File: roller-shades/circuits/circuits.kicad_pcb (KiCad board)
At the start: 2 copper layers, 40 x 55 mm, 38 parts, among them J1 USB_C_Receptacle_USB2.0, J2 SSD1306 connector, M1 Motor_DC, Q1 BC807, Q2 BC817, Q3 BC807, Q4 BC817, SW1 Rotary_Encoder_Switch, U1 AMS1117-3.3, U2 MCP9804_MSOP, U3 ESP-12F

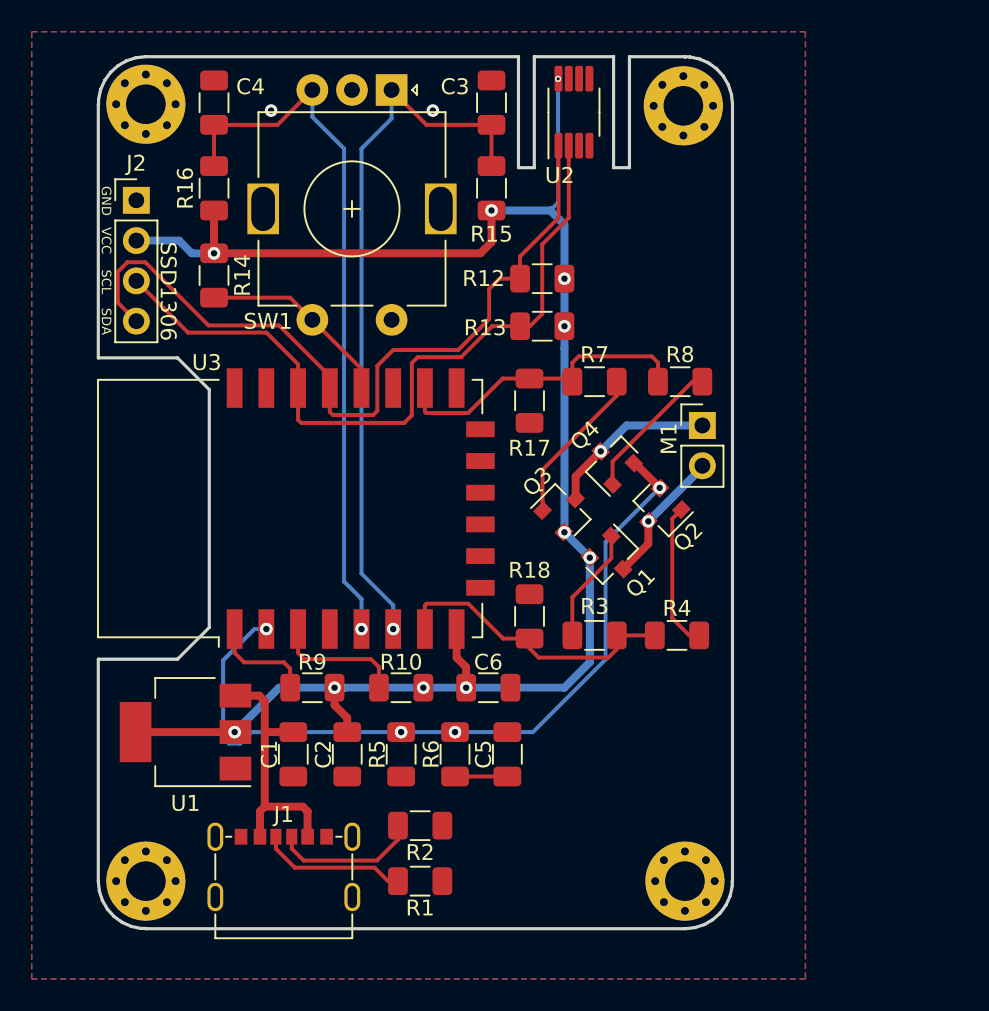
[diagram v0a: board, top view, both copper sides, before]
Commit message: working on driver board using kicad stepup for freecad
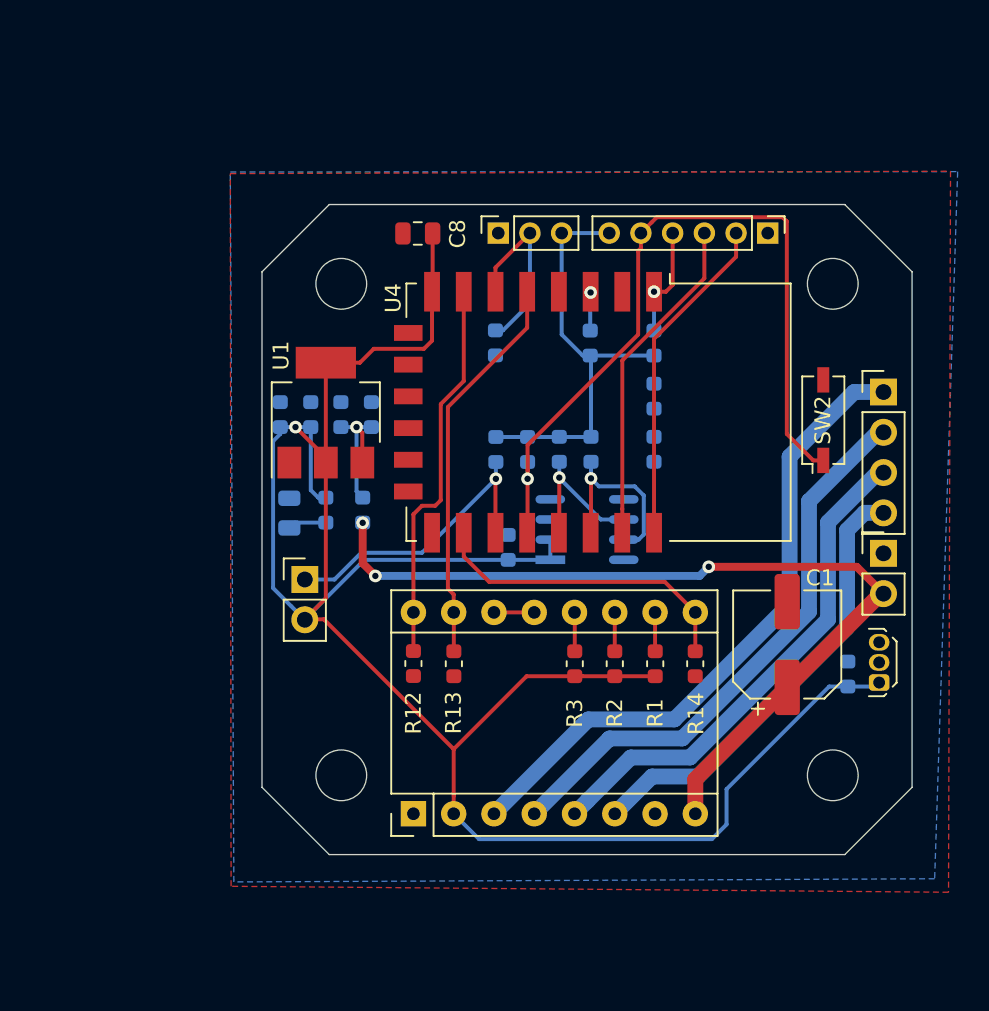
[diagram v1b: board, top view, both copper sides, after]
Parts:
- removed M1: Motor_DC, Connector_PinHeader_2.54mm:PinHeader_1x02_P2.54mm_Vertical
- removed Q1, Q3: BC807, Package_TO_SOT_SMD:SOT-23
- removed Q2, Q4: BC817, Package_TO_SOT_SMD:SOT-23
- removed R17, R18: 10K, Capacitor_SMD:C_1206_3216Metric
- removed REF** (x4): MountingHole_2.5mm_Pad_Via, MountingHole:MountingHole_2.5mm_Pad_Via
- removed SW1: Rotary_Encoder_Switch, Rotary_Encoder:RotaryEncoder_Alps_EC11E-Switch_Vertical_H20mm
- added A1: Pololu_Breakout_A4988, Module:Pololu_Breakout-16_15.2x20.3mm, F.Cu at (49.9, 70.2)
- added C7: 100nF, Capacitor_SMD:C_0603_1608Metric, B.Cu at (43.4, 45.1)
- added C8: 100nF, Fuse:Fuse_0805_2012Metric, F.Cu at (50.1, 33.6)
- added D1: DIODE, Diode_SMD:D_0805_2012Metric, B.Cu at (42.0, 51.3)
- added F1: Fuse, Fuse:Fuse_0603_1608Metric, B.Cu at (46.7, 51.1)
- added J3: PWR, Connector_PinHeader_2.54mm:PinHeader_1x02_P2.54mm_Vertical, F.Cu at (79.5, 53.8)
- added J4: PROG, Connector_PinHeader_2.00mm:PinHeader_1x06_P2.00mm_Vertical, F.Cu at (72.2, 33.6)
- added J5: WINDOW, Connector_PinHeader_2.54mm:PinHeader_1x02_P2.54mm_Vertical, F.Cu at (43.0, 55.5)
- added R11: 10k, Resistor_SMD:R_0603_1608Metric, B.Cu at (57.1, 47.3)
- added SW2: BTN_SW, Button_Switch_SMD:SW_DIP_SPSTx01_Slide_Copal_CHS-01A_W5.08mm_P1.27mm_JPin, F.Cu at (75.7, 45.4)
- added U4: ESP-12F, RF_Module:ESP-12E, F.Cu at (61.5, 44.9)
- C1: value 10µF -> 100µF; footprint Capacitor_SMD:C_1206_3216Metric -> Capacitor_SMD:CP_Elec_6.3x7.7
- C2: value 22µF -> 100nF; footprint Capacitor_SMD:C_1206_3216Metric -> Capacitor_SMD:C_0603_1608Metric; moved to B.Cu
- C3: value 10nF -> 10µF; footprint Capacitor_SMD:C_1206_3216Metric -> Capacitor_SMD:C_0603_1608Metric; moved to B.Cu
- C4: value 10nF -> 100nF; footprint Capacitor_SMD:C_1206_3216Metric -> Capacitor_SMD:C_0603_1608Metric; moved to B.Cu
- C5: value 100p -> 100nF; footprint Capacitor_SMD:C_1206_3216Metric -> Capacitor_SMD:C_0603_1608Metric; moved to B.Cu
- C6: value 100nF -> 10µF; footprint Capacitor_SMD:C_1206_3216Metric -> Capacitor_SMD:C_0603_1608Metric; moved to B.Cu
- J1: value USB_C_Receptacle_USB2.0 -> NEMA17; footprint Connector_USB:USB_C_Receptacle_SHOU_HAN_6P -> Connector_PinHeader_2.54mm:PinHeader_1x04_P2.54mm_Vertical
- J2: value SSD1306 connector -> DS18B20; footprint Connector_PinHeader_2.54mm:PinHeader_1x04_P2.54mm_Vertical -> Connector_PinSocket_2.00mm:PinSocket_1x03_P2.00mm_Vertical
- R1, R2: value 5K1 -> 10k; footprint Capacitor_SMD:C_1206_3216Metric -> Resistor_SMD:R_0603_1608Metric
- R10, R15, R16, R9: value 10K -> 10k; footprint Capacitor_SMD:C_1206_3216Metric -> Resistor_SMD:R_0603_1608Metric; moved to B.Cu
- R12, R13, R14: value 10K -> 10k; footprint Capacitor_SMD:C_1206_3216Metric -> Resistor_SMD:R_0603_1608Metric
- R3: value 1K -> 10k; footprint Capacitor_SMD:C_1206_3216Metric -> Resistor_SMD:R_0603_1608Metric
- R4, R8: value 1K -> 10k; footprint Capacitor_SMD:C_1206_3216Metric -> Resistor_SMD:R_0603_1608Metric; moved to B.Cu
- R5: value 20mR -> 220k; footprint Capacitor_SMD:C_1206_3216Metric -> Resistor_SMD:R_0603_1608Metric; moved to B.Cu
- R6: value 1K -> 100k; footprint Capacitor_SMD:C_1206_3216Metric -> Resistor_SMD:R_0603_1608Metric; moved to B.Cu
- R7: footprint Capacitor_SMD:C_1206_3216Metric -> Resistor_SMD:R_0603_1608Metric; moved to B.Cu
- U2: value MCP9804_MSOP -> AS5601-ASOM; footprint Package_SO:MSOP-8_3x3mm_P0.65mm -> AS5601:Taos-AS5601-ASOM-0-0-0; moved to B.Cu
- U3: value ESP-12F -> DRV5033A1; footprint RF_Module:ESP-12E -> Package_TO_SOT_THT:TO-92Flat
- moved J1 48.2 mm to (79.5, 43.6)
- moved R14 39.0 mm to (67.7, 60.8), turned to 90 degrees
- moved U3 38.7 mm to (79.2, 62.0)
- moved C1 31.9 mm to (73.5, 59.6), turned to 90 degrees
- moved R9 27.9 mm to (61.0, 40.6), turned to 90 degrees
- moved U2 26.3 mm to (60.8, 52.3), turned to 0 degrees
- moved R6 25.8 mm to (65.0, 43.9), turned to 90 degrees
- moved R12 25.6 mm to (49.9, 60.8), turned to 90 degrees
- moved R5 25.0 mm to (65.0, 47.3)
- moved J2 22.9 mm to (55.2, 33.6), turned to 90 degrees
- moved C5 22.1 mm to (77.3, 61.4)
- moved U1 22.0 mm to (44.4, 45.0), turned to 90 degrees
- moved R13 22.0 mm to (52.4, 60.8), turned to 90 degrees
- moved C6 21.7 mm to (41.5, 45.1), turned to 90 degrees
- moved C4 21.2 mm to (45.3, 45.1)
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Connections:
- C1 pad 1: +5V -> VDD
- C3 pad 1: /ESP_IO12 -> Net-(C3-Pad1)
- C4 pad 1: /ESP_IO14 -> Net-(C3-Pad1)
- C5 pad 1: Net-(C5-Pad1) -> +3V3
- J2 pad 2: +3V3 -> /GPIO12
- J2 pad 3: /ESP_IO5 -> +3V3
- R1 pad 1: Net-(J1-PadA5) -> +3V3
- R1 pad 2: GND -> /STPR_MS1
- R10 pad 2: /ESP_EN -> /I2C_SCL
- R12 pad 1: +3V3 -> GND
- R12 pad 2: /ESP_IO4 -> /STPR_DIR
- R13 pad 1: +3V3 -> GND
- R13 pad 2: /ESP_IO5 -> /STPR_STP
- R14 pad 1: +3V3 -> GND
- R14 pad 2: /ESP_IO0 -> /STPR_ENA
- R15 pad 2: /ESP_IO12 -> /GPIO2
- R16 pad 1: +3V3 -> GND
- R16 pad 2: /ESP_IO14 -> /GPIO12
- R2 pad 1: Net-(J1-PadB5) -> +3V3
- R2 pad 2: GND -> /STPR_MS2
- R3 pad 1: Net-(Q1-Pad1) -> +3V3
- R3 pad 2: /ESP_IO13 -> /STPR_MS3
- R4 pad 1: Net-(Q2-Pad1) -> +3V3
- R4 pad 2: /ESP_IO13 -> /I2C_SDA
- R5 pad 1: GND -> Net-(R5-Pad1)
- R5 pad 2: /ESP_ADC -> /GPIO_ADC
- R6 pad 1: /ESP_ADC -> /GPIO_ADC
- R6 pad 2: Net-(C5-Pad1) -> GND
- R7 pad 1: /ESP_IO15 -> Net-(D1-Pad1)
- R7 pad 2: Net-(Q3-Pad1) -> +3V3
- R8 pad 1: /ESP_IO15 -> +3V3
- R8 pad 2: Net-(Q4-Pad1) -> /RST
- R9 pad 2: /ESP_RST -> Net-(R9-Pad2)
- U1 pad 3: +5V -> Net-(C3-Pad1)
- U2 pad 1: /ESP_IO4 -> +3V3
- U2 pad 2: /ESP_IO5 -> +3V3
- U2 pad 6: Net-(U2-Pad6) -> /I2C_SDA
- U2 pad 7: Net-(U2-Pad7) -> /I2C_SCL
- U2 pad 8: +3V3 -> Net-(U2-Pad8)
- U3 pad 1: /ESP_RST -> +3V3
- U3 pad 2: /ESP_ADC -> Net-(R5-Pad1)
- U3 pad 3: /ESP_EN -> GND
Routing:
- net +3V3: track 107.1 -> 163.6 mm, vias 11 -> 1
- net VDD: track 0.00 -> 55.6 mm, vias 0 -> 3
- net /ESP_IO4: track 50.3 -> 0.00 mm
- net /ESP_ADC: track 49.4 -> 0.00 mm, vias 4 -> 0
- net /GPIO0: track 0.00 -> 49.1 mm, vias 0 -> 1
- net /ESP_IO5: track 47.4 -> 0.00 mm
- net /ESP_IO12: track 45.4 -> 0.00 mm, vias 1 -> 0
- net /ESP_IO14: track 45.0 -> 0.00 mm, vias 1 -> 0
- net Net-(A1-Pad3): track 0.00 -> 41.0 mm
- net Net-(A1-Pad4): track 0.00 -> 36.1 mm
- net Net-(A1-Pad5): track 0.00 -> 32.0 mm
- net Net-(A1-Pad6): track 0.00 -> 28.4 mm
- net /STPR_STP: track 0.00 -> 24.9 mm
- net /STPR_DIR: track 0.00 -> 24.5 mm
- net /TXD: track 0.00 -> 21.0 mm
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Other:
- board size 40 x 55 mm -> 41 x 41 mm
- board text added: "www.github.com/slimcdk/ smart-home-projects.git"
- board text removed: "GND"
- board text removed: "SCL"
- board text removed: "SDA"
- board text removed: "SSD1306"
- board text removed: "VCC"
- board text removed: "eQ3-ESPMOD | v0.2 github.com/slimcdk/eq3-espmod slimc | February 2020"
